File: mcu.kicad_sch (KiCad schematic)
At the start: 17 parts, among them U1 STM32F303RETx, U8 AZ1117-3.3

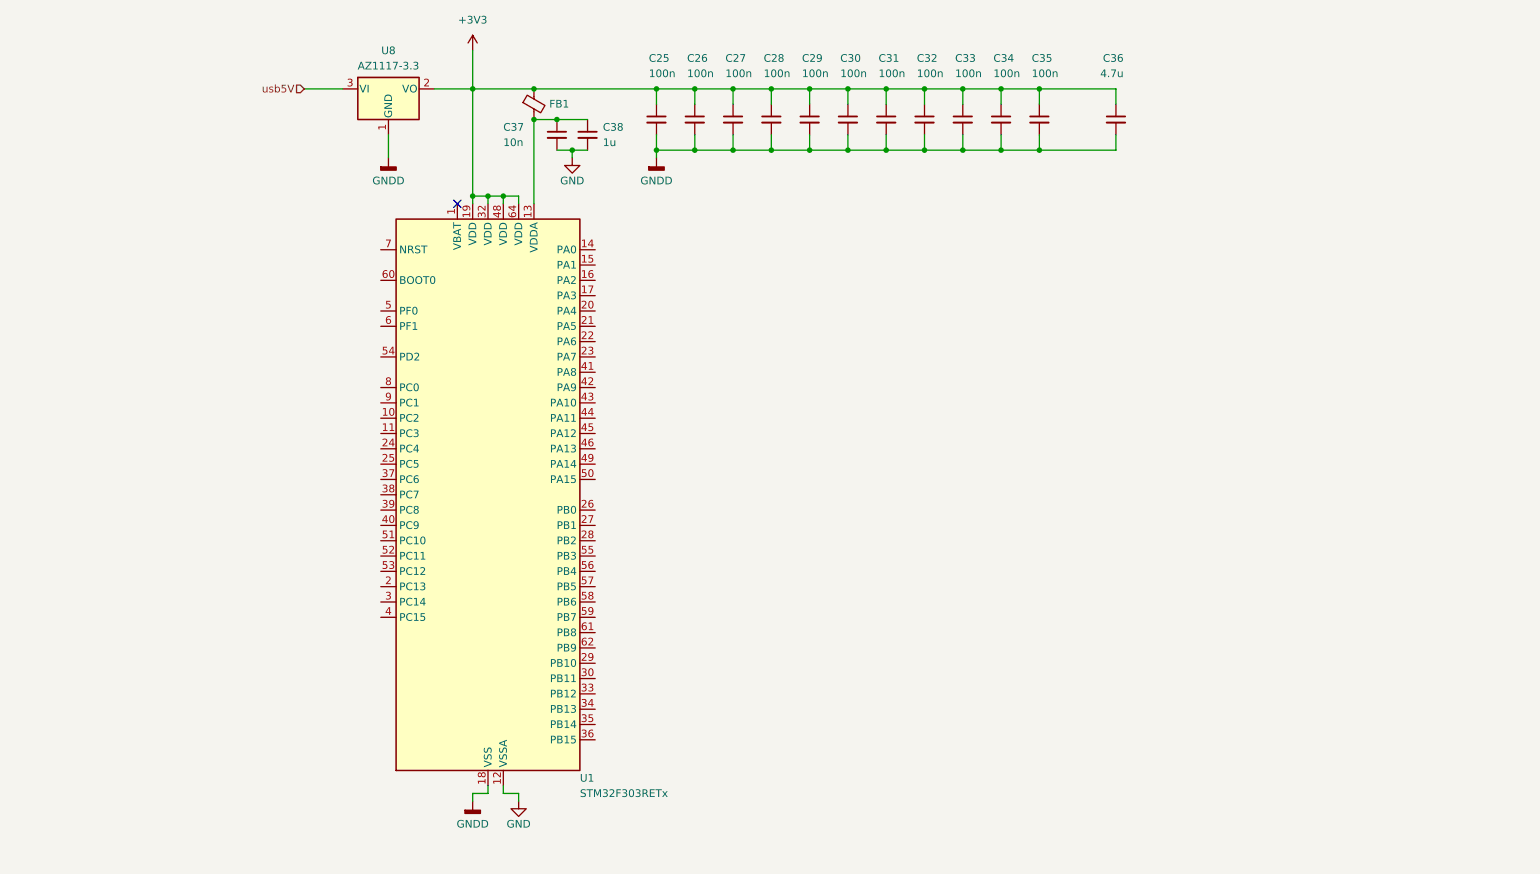
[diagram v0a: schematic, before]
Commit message: cleanup decoupling caps
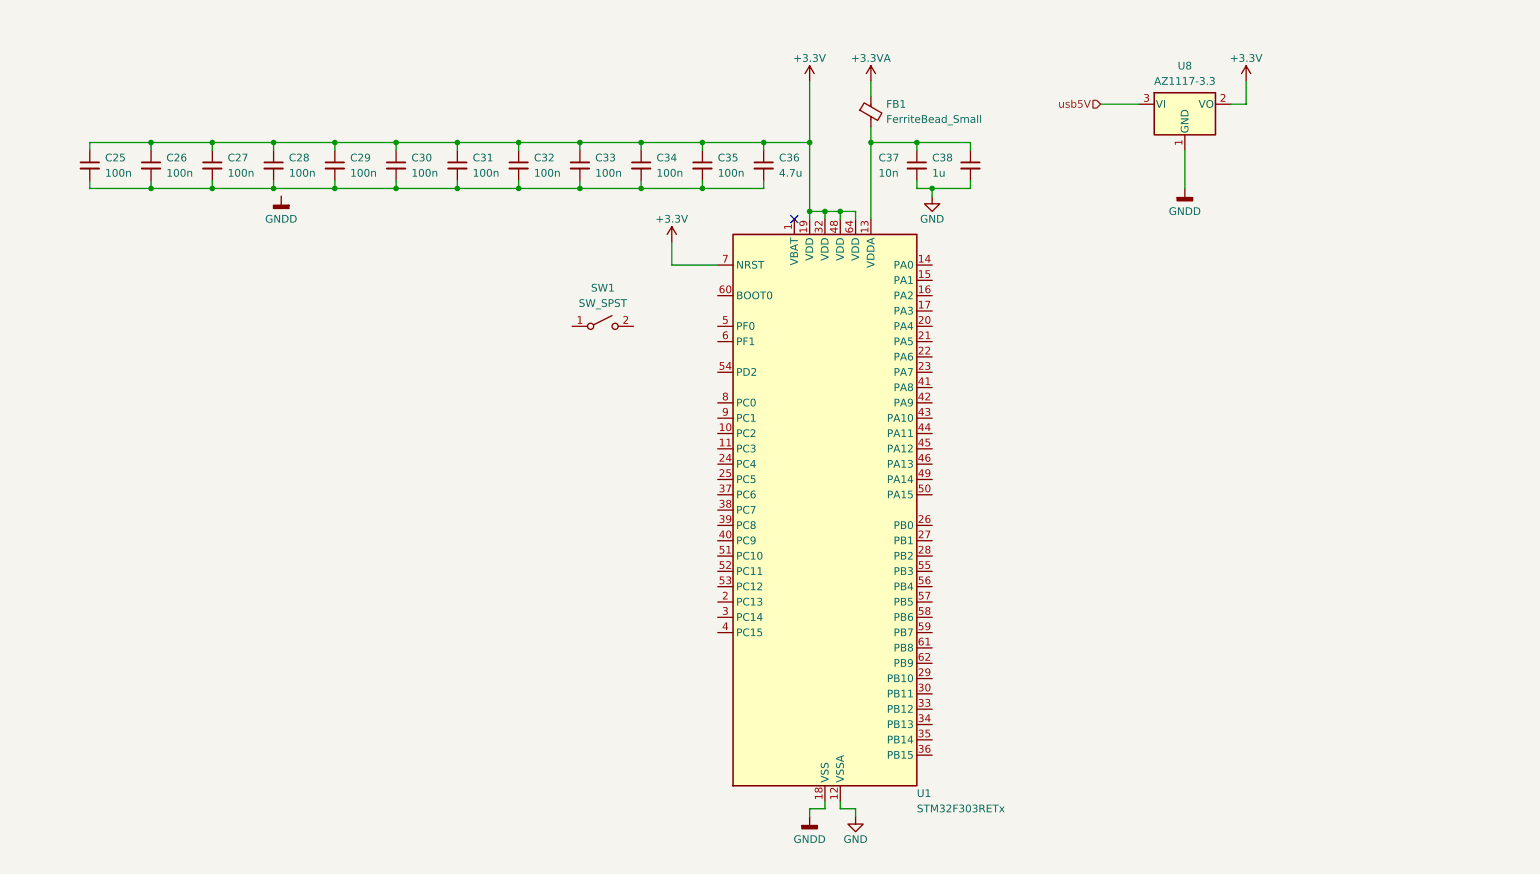
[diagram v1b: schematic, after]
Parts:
- added SW1: SW_SPST, symbol Switch:SW_SPST
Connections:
- net GNDD: no longer C25.2, C26.2, C27.2, C28.2, C29.2, C30.2, C31.2, C32.2, C33.2, C34.2, C35.2, C36.2
- net +3.3V: now reaches U1.7 (NRST)
- net +3.3V: now also C25.1, C26.1, C27.1, C28.1, C29.1, C30.1, C31.1, C32.1, C33.1, C34.1, C35.1, C36.1, U1.19 (VDD), U1.32 (VDD), U1.48 (VDD), U1.64 (VDD), U8.2 (VO)
- removed net +3V3: C25.1, C26.1, C27.1, C28.1, C29.1, C30.1, C31.1, C32.1, C33.1, C34.1, C35.1, C36.1, FB1.1, U1.19 (VDD), U1.32 (VDD), U1.48 (VDD), U1.64 (VDD), U8.2 (VO)
- new net: C25.2, C26.2, C27.2, C28.2, C29.2, C30.2, C31.2, C32.2, C33.2, C34.2, C35.2, C36.2
- new net +3.3VA: FB1.1
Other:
- moved on the sheet: C25, C26, C27, C28, C29, C30, C31, C32, C33, C34, C35, C36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

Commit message: finish initial supporting components for mcu
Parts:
- removed SW1: SW_SPST, symbol Switch:SW_SPST
- added C39: 100n, symbol Device:C_Small
- added C40, C41: 20p, symbol Device:C_Small
- added J20: Conn_01x04_Socket, symbol Connector:Conn_01x04_Socket
- added R75: 10k, symbol Device:R
- added R76: 390, symbol Device:R
- added SW1: SW_Push, symbol Switch:SW_Push
- added SW2: SW_SPDT, symbol Switch:SW_SPDT
- added Y1: 8M, symbol Device:Crystal
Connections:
- net +3.3V: now also U1.1 (VBAT), J20.3 (Pin_3), SW2.3 (C); no longer U1.7 (NRST)
- net GNDD: now also C25.2, C26.2, C27.2, C28.2, C29.2, C30.2, C31.2, C32.2, C33.2, C34.2, C35.2, C36.2, C39.2, C40.1, C41.1, J20.4 (Pin_4), SW1.1, SW2.1 (A)
- net spi0clk: now reaches U1.21 (PA5)
- net spi0miso: now reaches U1.22 (PA6)
- net spi0mosi: now reaches U1.23 (PA7)
- net linectrl15: now reaches U1.24 (PC4)
- net linectrl6: now reaches U1.27 (PB1)
- net linectrl4: now reaches U1.28 (PB2)
- net linectrl7: now reaches U1.29 (PB10)
- net linectrl1: now reaches U1.30 (PB11)
- net linectrl12: now reaches U1.34 (PB13)
- net linectrl10: now reaches U1.35 (PB14)
- net linectrl8: now reaches U1.36 (PB15)
- net linectrl2: now reaches U1.38 (PC7)
- net linectrl5: now reaches U1.41 (PA8)
- net linectrl3: now reaches U1.42 (PA9)
- net linectrl14: now reaches U1.43 (PA10)
- net spi0cs0: now reaches U1.45 (PA12)
- net SWDIO: now reaches U1.46 (PA13)
- net SWDIO: now also J20.1 (Pin_1)
- net SWCLK: now reaches U1.49 (PA14)
- net SWCLK: now also J20.2 (Pin_2)
- net at U1.5 (PF0): now also C40.2, Y1.2
- net shiftOut: now reaches U1.51 (PC10)
- net shiftClk: now reaches U1.52 (PC11)
- net shiftInh: now reaches U1.53 (PC12)
- net shiftLd: now reaches U1.54 (PD2)
- net linectrl13: now reaches U1.55 (PB3)
- net linectrl9: now reaches U1.56 (PB4)
- net linectrl11: now reaches U1.57 (PB5)
- net linectrl0: now reaches U1.58 (PB6)
- net at U1.6 (PF1): now also R76.2
- net at U1.60 (BOOT0): now also R75.2
- new net: C39.1, SW1.2, U1.7 (NRST)
- new net: C41.2, R76.1, Y1.1
- new net: R75.1, SW2.2 (B)
- no-connect marks 1 -> 0
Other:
- note added: "3.3V LDO Regulator"
- note added: "Boot Mode Selection Switch"
- note added: "Ext. 8MHz Crystal Oscillator"
- note added: "Reset Button"
- note added: "SWD Connector"

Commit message: fix nearly all erc errors
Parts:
- added J21: Conn_01x03_Socket, symbol Connector:Conn_01x03_Socket
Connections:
- net +3.3V: now also FB1.2
- net +3.3VA: now also C37.1, C38.1, U1.13 (VDDA)
- net GNDD: now also J21.3 (Pin_3)
- net USART2_TX: now reaches U1.16 (PA2)
- net USART2_TX: now also J21.1 (Pin_1)
- net USART2_RX: now reaches U1.17 (PA3)
- net USART2_RX: now also J21.2 (Pin_2)
- net usbD-: now reaches U1.44 (PA11)
- net spi0cs0 renamed usbD+
- no-connect marks 0 -> 20
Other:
- note added: "UART Connector"
- moved on the sheet: J20, U8

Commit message: unsplit grounds, finish power circuitry, start picking footprints/partnumbers
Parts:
- removed FB1: FerriteBead_Small, symbol Device:FerriteBead_Small
- removed U8: AZ1117-3.3, symbol Regulator_Linear:AZ1117-3.3
- C25, C26, C27, C28, C29, C30, C31, C32, C33, C34, C35, C36, C37, C38, C39, C40, C41: footprint (none) -> Capacitor_SMD:C_0805_2012Metric
- J20: footprint (none) -> Connector_PinHeader_2.54mm:PinHeader_1x04_P2.54mm_Vertical
- J21: footprint (none) -> Connector_PinHeader_2.54mm:PinHeader_1x03_P2.54mm_Vertical
- R75, R76: footprint (none) -> Resistor_SMD:R_0805_2012Metric
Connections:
- net GNDD is gone; now on net GND: C25.2, C26.2, C27.2, C28.2, C29.2, C30.2, C31.2, C32.2, C33.2, C34.2, C35.2, C36.2, C39.2, C40.1, C41.1, J20.4 (Pin_4), J21.3 (Pin_3), SW1.1, SW2.1 (A), U1.18 (VSS), U1.31 (VSS), U1.47 (VSS), U1.63 (VSS)
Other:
- note removed: "3.3V LDO Regulator"

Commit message: added power mux, finished up schematic and picking footprints/partnumbers
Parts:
- C7: renamed from C40; value 20p -> 22p
- C8: renamed from C41; value 20p -> 22p
- SW1: renamed from SW2; footprint (none) -> Button_Switch_SMD:SW_SPDT_CK_JS102011SAQN; DKPN (none) -> 401-1999-1-ND
- SW2: renamed from SW1; footprint (none) -> Button_Switch_SMD:SW_SPST_PTS647_Sx50; DKPN (none) -> 108-PTS647SM50SMTR2LFSCT-ND
- Y1: footprint (none) -> Crystal:Crystal_SMD_Abracon_ABM3-2Pin_5.0x3.2mm_HandSoldering; DKPN (none) -> 535-10630-1-ND
- renumbered C25 to C1, C31 to C10, C32 to C11, C33 to C12, C34 to C13, C35 to C14, C36 to C15, C37 to C16, C38 to C17, C26 to C2, C27 to C3, C39 to C4, C28 to C5, C29 to C6, C30 to C9, J20 to J3, J21 to J4, R75 to R5, R76 to R6, U1 to U3
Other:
- note added: "Connectors"
- note added: "Decoupling Caps"
- note added: "Main MCU Circuitry"
